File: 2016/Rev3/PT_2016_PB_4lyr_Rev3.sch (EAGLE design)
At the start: 169 parts, among them Q1 MOSFET-NCHANNELFDD8780, Q12 2N7002, Q3 MOSFET-NCHANNELFDD8780, Q4 MMBT2222A, Q5 MMBT4403

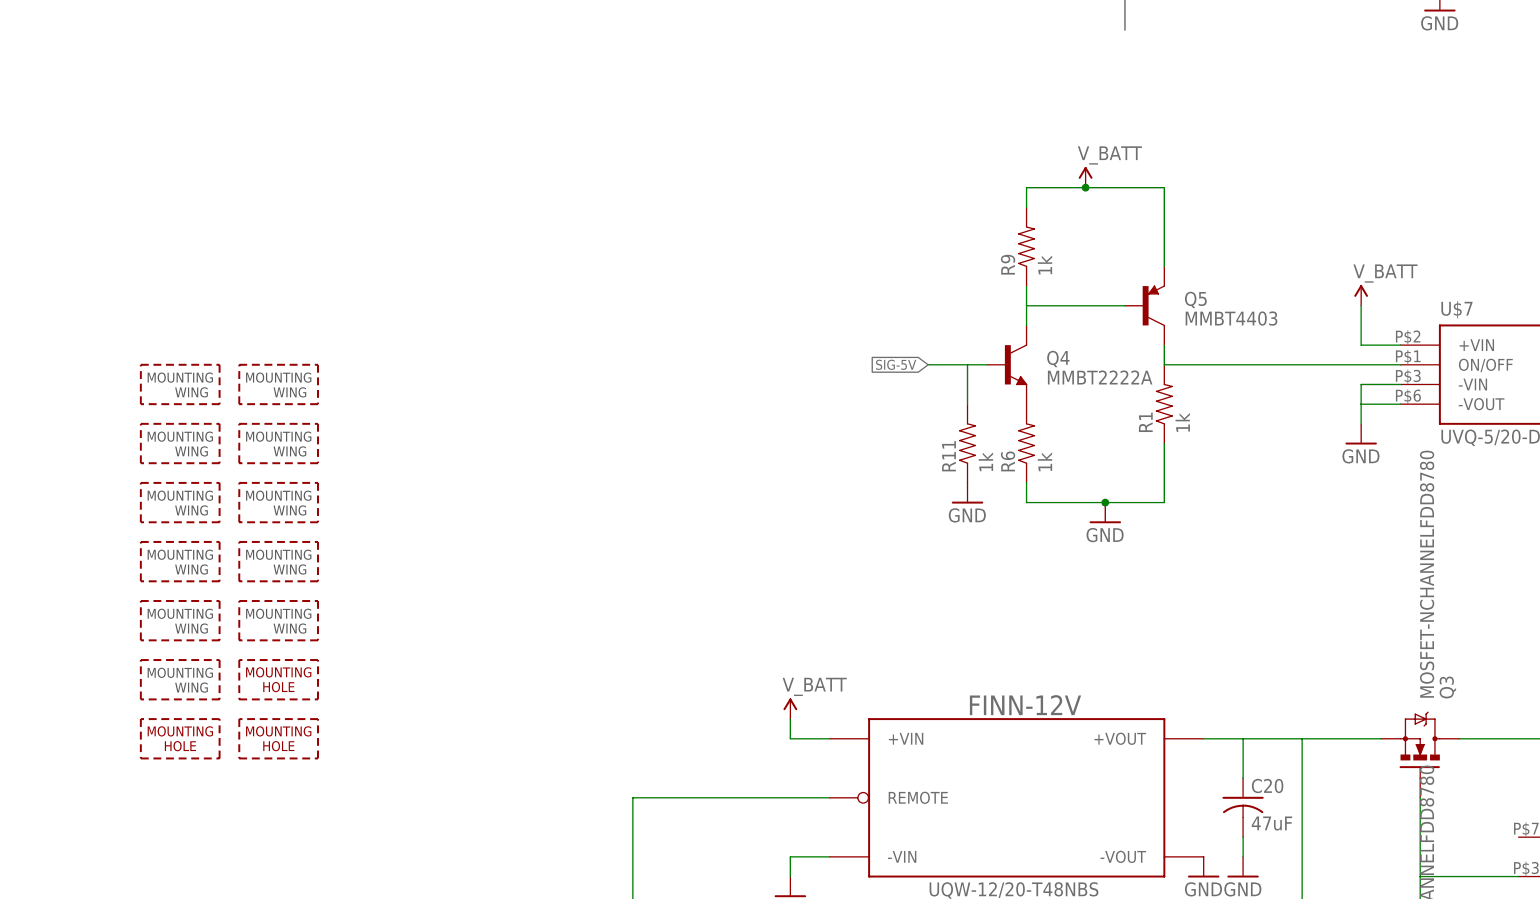
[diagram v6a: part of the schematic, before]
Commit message: Changed 5V on/off circuit, enlarged planes
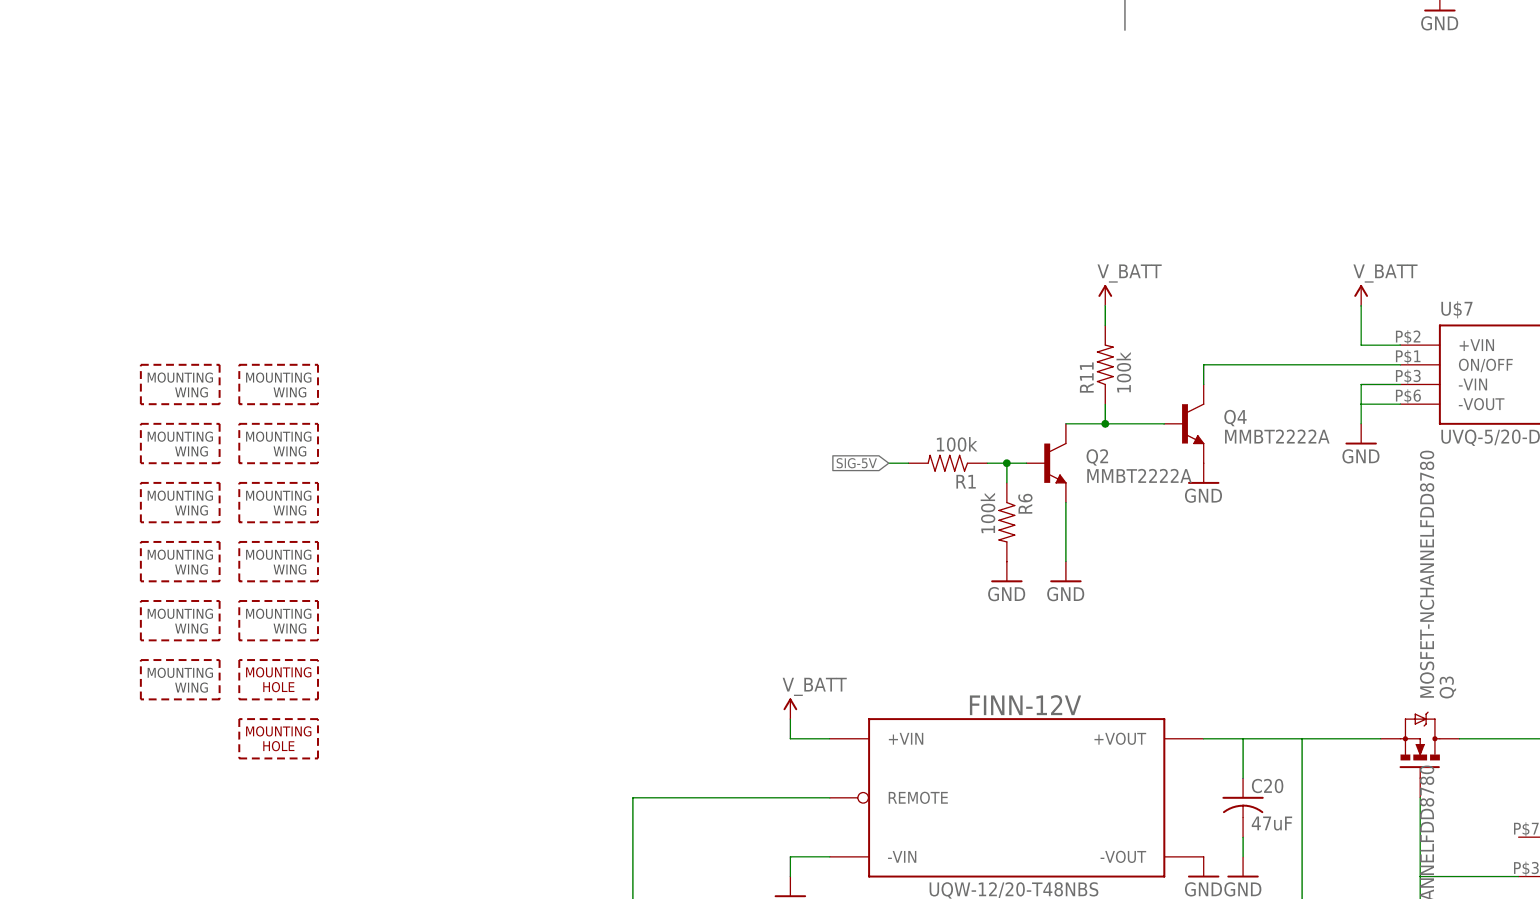
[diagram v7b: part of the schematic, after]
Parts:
- removed Q5: MMBT4403, SparkFun-DiscreteSemi:TRANSISTOR_PNPMMBT4403
- removed R9: 1k, SparkFun-Passives:RESISTOR1206
- removed U$11: MOUNTING_HOLE#8, MRDT-Hardware:MOUNTING_HOLE#8
- added Q2: MMBT2222A, SparkFun-DiscreteSemi:TRANSISTOR_NPNMMBT2222A
- R1, R11, R6: value 1k -> 100k
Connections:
- removed net N$43: Q5.C, R1.2, U$7.ON/OFF
- new net N$14: Q2.B, R1.1, R6.1
- net GND: now also Q2.E, Q4.E, R6.2; no longer R1.1, R11.1, R6.1
- net N$11: now also U$7.ON/OFF; no longer Q5.B, R9.1
- net N$15: now also Q2.C, Q4.B, R11.1; no longer Q4.E, R6.2
- net SIG-5V: now also R1.2; no longer Q4.B, R11.2
- net V_BATT: now also R11.2; no longer Q5.E, R9.2
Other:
- moved on the sheet: Q4, R1, R11, R6
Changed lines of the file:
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@@
 <part name="U$8" library="MRDT-Hardware" deviceset="MOUNTING_HOLE" device="#8"/>
 <part name="U$10" library="MRDT-Hardware" deviceset="MOUNTING_HOLE" device="#8"/>
-<part name="U$11" library="MRDT-Hardware" deviceset="MOUNTING_HOLE" device="#8"/>
 <part name="U$7" library="MRDT-2015-PowerBoard" deviceset="UVQ-5/20-D24PB-C" device=""/>
 <part name="SUPPLY18" library="SparkFun-Aesthetics" deviceset="3.3V" device=""/>
@@
 <part name="SUPPLY31" library="SparkFun-Aesthetics" deviceset="5V" device=""/>
 <part name="Q4" library="SparkFun-DiscreteSemi" deviceset="TRANSISTOR_NPN" device="MMBT2222A" value="MMBT2222A"/>
-<part name="Q5" library="SparkFun-DiscreteSemi" deviceset="TRANSISTOR_PNP" device="MMBT4403" value="MMBT4403"/>
-<part name="R1" library="SparkFun-Passives" deviceset="RESISTOR" device="1206" value="1k"/>
-<part name="R6" library="SparkFun-Passives" deviceset="RESISTOR" device="1206" value="1k"/>
-<part name="R9" library="SparkFun-Passives" deviceset="RESISTOR" device="1206" value="1k"/>
 <part name="SUPPLY32" library="SparkFun-Aesthetics" deviceset="V_BATT" device=""/>
 <part name="GND16" library="SparkFun-Aesthetics" deviceset="GND" device=""/>
-<part name="R11" library="SparkFun-Passives" deviceset="RESISTOR" device="1206" value="1k"/>
+<part name="R11" library="SparkFun-Passives" deviceset="RESISTOR" device="1206" value="100k"/>
+<part name="Q2" library="SparkFun-DiscreteSemi" deviceset="TRANSISTOR_NPN" device="MMBT2222A" value="MMBT2222A"/>
 <part name="GND17" library="SparkFun-Aesthetics" deviceset="GND" device=""/>
+<part name="R1" library="SparkFun-Passives" deviceset="RESISTOR" device="1206" value="100k"/>
+<part name="R6" library="SparkFun-Passives" deviceset="RESISTOR" device="1206" value="100k"/>
+<part name="GND35" library="SparkFun-Aesthetics" deviceset="GND" device=""/>
 </parts>
 <sheets>
@@
 <instance part="U$8" gate="G$1" x="-149.86" y="86.36"/>
 <instance part="U$10" gate="G$1" x="-149.86" y="78.74"/>
-<instance part="U$11" gate="G$1" x="-162.56" y="78.74"/>
 <instance part="U$7" gate="G$1" x="15.24" y="129.54"/>
 <instance part="SUPPLY18" gate="G$1" x="-22.86" y="-30.48"/>
@@
 <instance part="C10" gate="G$1" x="63.5" y="20.32"/>
 <instance part="SUPPLY31" gate="G$1" x="200.66" y="-76.2"/>
-<instance part="Q4" gate="G$1" x="-50.8" y="129.54"/>
-<instance part="Q5" gate="G$1" x="-33.02" y="137.16"/>
-<instance part="R1" gate="G$1" x="-30.48" y="124.46" rot="R90"/>
-<instance part="R6" gate="G$1" x="-48.26" y="119.38" rot="R90"/>
-<instance part="R9" gate="G$1" x="-48.26" y="144.78" rot="R90"/>
-<instance part="SUPPLY32" gate="G$1" x="-40.64" y="152.4"/>
-<instance part="GND16" gate="1" x="-38.1" y="109.22"/>
-<instance part="R11" gate="G$1" x="-55.88" y="119.38" rot="R90"/>
-<instance part="GND17" gate="1" x="-55.88" y="111.76"/>
+<instance part="Q4" gate="G$1" x="-27.94" y="121.92"/>
+<instance part="SUPPLY32" gate="G$1" x="-38.1" y="137.16"/>
+<instance part="GND16" gate="1" x="-43.18" y="101.6"/>
+<instance part="R11" gate="G$1" x="-38.1" y="129.54" rot="R90"/>
+<instance part="Q2" gate="G$1" x="-45.72" y="116.84"/>
+<instance part="GND17" gate="1" x="-25.4" y="114.3"/>
+<instance part="R1" gate="G$1" x="-58.42" y="116.84" rot="R180"/>
+<instance part="R6" gate="G$1" x="-50.8" y="109.22" rot="R270"/>
+<instance part="GND35" gate="1" x="-50.8" y="101.6"/>
 </instances>
 <busses>
@@
 </segment>
 <segment>
-<pinref part="R1" gate="G$1" pin="1"/>
-<wire x1="-30.48" y1="119.38" x2="-30.48" y2="111.76" width="0.1524" layer="91"/>
-<pinref part="R6" gate="G$1" pin="1"/>
-<wire x1="-30.48" y1="111.76" x2="-38.1" y2="111.76" width="0.1524" layer="91"/>
-<wire x1="-38.1" y1="111.76" x2="-48.26" y2="111.76" width="0.1524" layer="91"/>
-<wire x1="-48.26" y1="111.76" x2="-48.26" y2="114.3" width="0.1524" layer="91"/>
+<pinref part="Q4" gate="G$1" pin="E"/>
+<pinref part="GND17" gate="1" pin="GND"/>
+</segment>
+<segment>
+<pinref part="Q2" gate="G$1" pin="E"/>
 <pinref part="GND16" gate="1" pin="GND"/>
-<junction x="-38.1" y="111.76"/>
-</segment>
-<segment>
-<pinref part="R11" gate="G$1" pin="1"/>
-<pinref part="GND17" gate="1" pin="GND"/>
+<wire x1="-43.18" y1="104.14" x2="-43.18" y2="111.76" width="0.1524" layer="91"/>
+</segment>
+<segment>
+<pinref part="R6" gate="G$1" pin="2"/>
+<pinref part="GND35" gate="1" pin="GND"/>
 </segment>
 </net>
@@
 </segment>
 <segment>
-<pinref part="Q5" gate="G$1" pin="E"/>
-<wire x1="-30.48" y1="142.24" x2="-30.48" y2="152.4" width="0.1524" layer="91"/>
-<wire x1="-30.48" y1="152.4" x2="-40.64" y2="152.4" width="0.1524" layer="91"/>
-<pinref part="R9" gate="G$1" pin="2"/>
-<wire x1="-40.64" y1="152.4" x2="-48.26" y2="152.4" width="0.1524" layer="91"/>
-<wire x1="-48.26" y1="152.4" x2="-48.26" y2="149.86" width="0.1524" layer="91"/>
+<pinref part="R11" gate="G$1" pin="2"/>
 <pinref part="SUPPLY32" gate="G$1" pin="V_BATT"/>
-<junction x="-40.64" y="152.4"/>
+<wire x1="-38.1" y1="137.16" x2="-38.1" y2="134.62" width="0.1524" layer="91"/>
 </segment>
 </net>
@@
 </segment>
 </net>
-<net name="N$43" class="0">
-<segment>
-<wire x1="0" y1="129.54" x2="-30.48" y2="129.54" width="0.1524" layer="91"/>
-<pinref part="U$7" gate="G$1" pin="ON/OFF"/>
-<pinref part="Q5" gate="G$1" pin="C"/>
+<net name="SIG-5V" class="0">
+<segment>
+<label x="-66.04" y="116.84" size="1.27" layer="95" rot="R180" xref="yes"/>
 <pinref part="R1" gate="G$1" pin="2"/>
-<wire x1="-30.48" y1="129.54" x2="-30.48" y2="132.08" width="0.1524" layer="91"/>
-</segment>
-</net>
-<net name="SIG-5V" class="0">
-<segment>
-<wire x1="-53.34" y1="129.54" x2="-55.88" y2="129.54" width="0.1524" layer="91"/>
-<label x="-60.96" y="129.54" size="1.27" layer="95" rot="R180" xref="yes"/>
-<pinref part="Q4" gate="G$1" pin="B"/>
-<pinref part="R11" gate="G$1" pin="2"/>
-<wire x1="-55.88" y1="129.54" x2="-60.96" y2="129.54" width="0.1524" layer="91"/>
-<wire x1="-55.88" y1="124.46" x2="-55.88" y2="129.54" width="0.1524" layer="91"/>
+<wire x1="-63.5" y1="116.84" x2="-66.04" y2="116.84" width="0.1524" layer="91"/>
 </segment>
 <segment>
@@
 <net name="N$11" class="0">
 <segment>
-<pinref part="Q5" gate="G$1" pin="B"/>
-<wire x1="-35.56" y1="137.16" x2="-48.26" y2="137.16" width="0.1524" layer="91"/>
+<pinref part="U$7" gate="G$1" pin="ON/OFF"/>
 <pinref part="Q4" gate="G$1" pin="C"/>
-<wire x1="-48.26" y1="137.16" x2="-48.26" y2="134.62" width="0.1524" layer="91"/>
-<pinref part="R9" gate="G$1" pin="1"/>
-<wire x1="-48.26" y1="139.7" x2="-48.26" y2="137.16" width="0.1524" layer="91"/>
+<wire x1="0" y1="129.54" x2="-25.4" y2="129.54" width="0.1524" layer="91"/>
+<wire x1="-25.4" y1="129.54" x2="-25.4" y2="127" width="0.1524" layer="91"/>
+</segment>
+</net>
+<net name="N$14" class="0">
+<segment>
+<pinref part="Q2" gate="G$1" pin="B"/>
+<pinref part="R1" gate="G$1" pin="1"/>
+<wire x1="-53.34" y1="116.84" x2="-50.8" y2="116.84" width="0.1524" layer="91"/>
+<pinref part="R6" gate="G$1" pin="1"/>
+<wire x1="-50.8" y1="116.84" x2="-48.26" y2="116.84" width="0.1524" layer="91"/>
+<wire x1="-50.8" y1="114.3" x2="-50.8" y2="116.84" width="0.1524" layer="91"/>
+<junction x="-50.8" y="116.84"/>
 </segment>
 </net>
 <net name="N$15" class="0">
 <segment>
-<pinref part="Q4" gate="G$1" pin="E"/>
-<pinref part="R6" gate="G$1" pin="2"/>
-</segment>
-</net>
+<pinref part="Q4" gate="G$1" pin="B"/>
+<pinref part="R11" gate="G$1" pin="1"/>
+<wire x1="-30.48" y1="121.92" x2="-38.1" y2="121.92" width="0.1524" layer="91"/>
+<wire x1="-38.1" y1="121.92" x2="-38.1" y2="124.46" width="0.1524" layer="91"/>
+<pinref part="Q2" gate="G$1" pin="C"/>
+<wire x1="-43.18" y1="121.92" x2="-38.1" y2="121.92" width="0.1524" layer="91"/>
+<junction x="-38.1" y="121.92"/>
+</segment>
+</net>

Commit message: Cleaned up some routing/planes
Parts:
- R5: value 1k -> 100k
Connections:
- removed net N$100: U$1.RST
- removed net N$101: U$1.PB2
- removed net N$102: U$1.PB3
- removed net N$110: U$1.PD5
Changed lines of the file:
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@@
 <part name="GND86" library="SparkFun-Aesthetics" deviceset="GND" device=""/>
 <part name="SUPPLY30" library="SparkFun-Aesthetics" deviceset="5V" device=""/>
-<part name="R5" library="resistor" deviceset="R-US_" device="R1206" value="1k"/>
+<part name="R5" library="resistor" deviceset="R-US_" device="R1206" value="100k"/>
 <part name="GND91" library="SparkFun-Aesthetics" deviceset="GND" device=""/>
 <part name="U$9" library="LM74670-Q1" deviceset="LM74670-Q1" device=""/>
@@
 </segment>
 </net>
-<net name="N$100" class="0">
-<segment>
-<wire x1="-132.08" y1="-43.18" x2="-127" y2="-43.18" width="0.1524" layer="91"/>
-<pinref part="U$1" gate="G$1" pin="RST"/>
-</segment>
-</net>
-<net name="N$101" class="0">
-<segment>
-<wire x1="-132.08" y1="-48.26" x2="-127" y2="-48.26" width="0.1524" layer="91"/>
-<pinref part="U$1" gate="G$1" pin="PB2"/>
-</segment>
-</net>
-<net name="N$102" class="0">
-<segment>
-<wire x1="-132.08" y1="-50.8" x2="-127" y2="-50.8" width="0.1524" layer="91"/>
-<pinref part="U$1" gate="G$1" pin="PB3"/>
-</segment>
-</net>
-<net name="N$110" class="0">
-<segment>
-<wire x1="-132.08" y1="-73.66" x2="-127" y2="-73.66" width="0.1524" layer="91"/>
-<pinref part="U$1" gate="G$1" pin="PD5"/>
-</segment>
-</net>
